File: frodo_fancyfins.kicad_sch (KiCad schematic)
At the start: 64 parts, among them J1 Molex MicroFit 2x3, J2 Molex MicroFit 2x3, J3 U.FL, J4 SWD Header, Q1 AO3400A, U15 AZ1117-5.0, U16 AZ1117-5.0, U17 W25Q128JVP, U18 AS321KTR-G1, U2 MCP2562-E-SN, U3 AZ1117-3.3, U4 STM32F103RCTx, Y1 8MHz 12pF

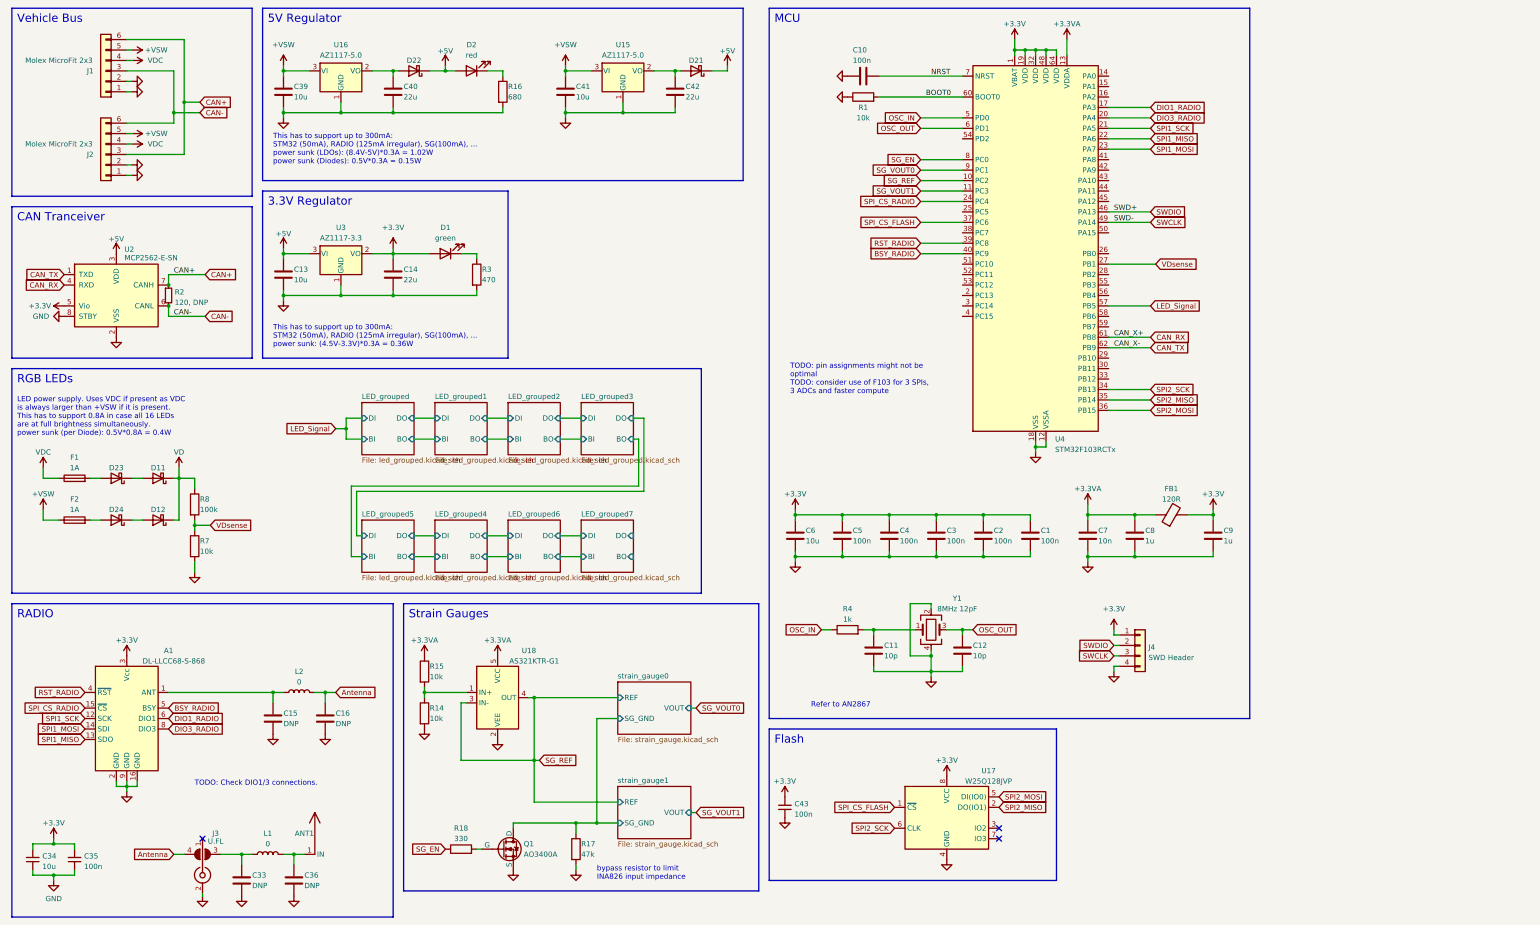
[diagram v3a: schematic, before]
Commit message: implement changes from rev 0 to rev 1
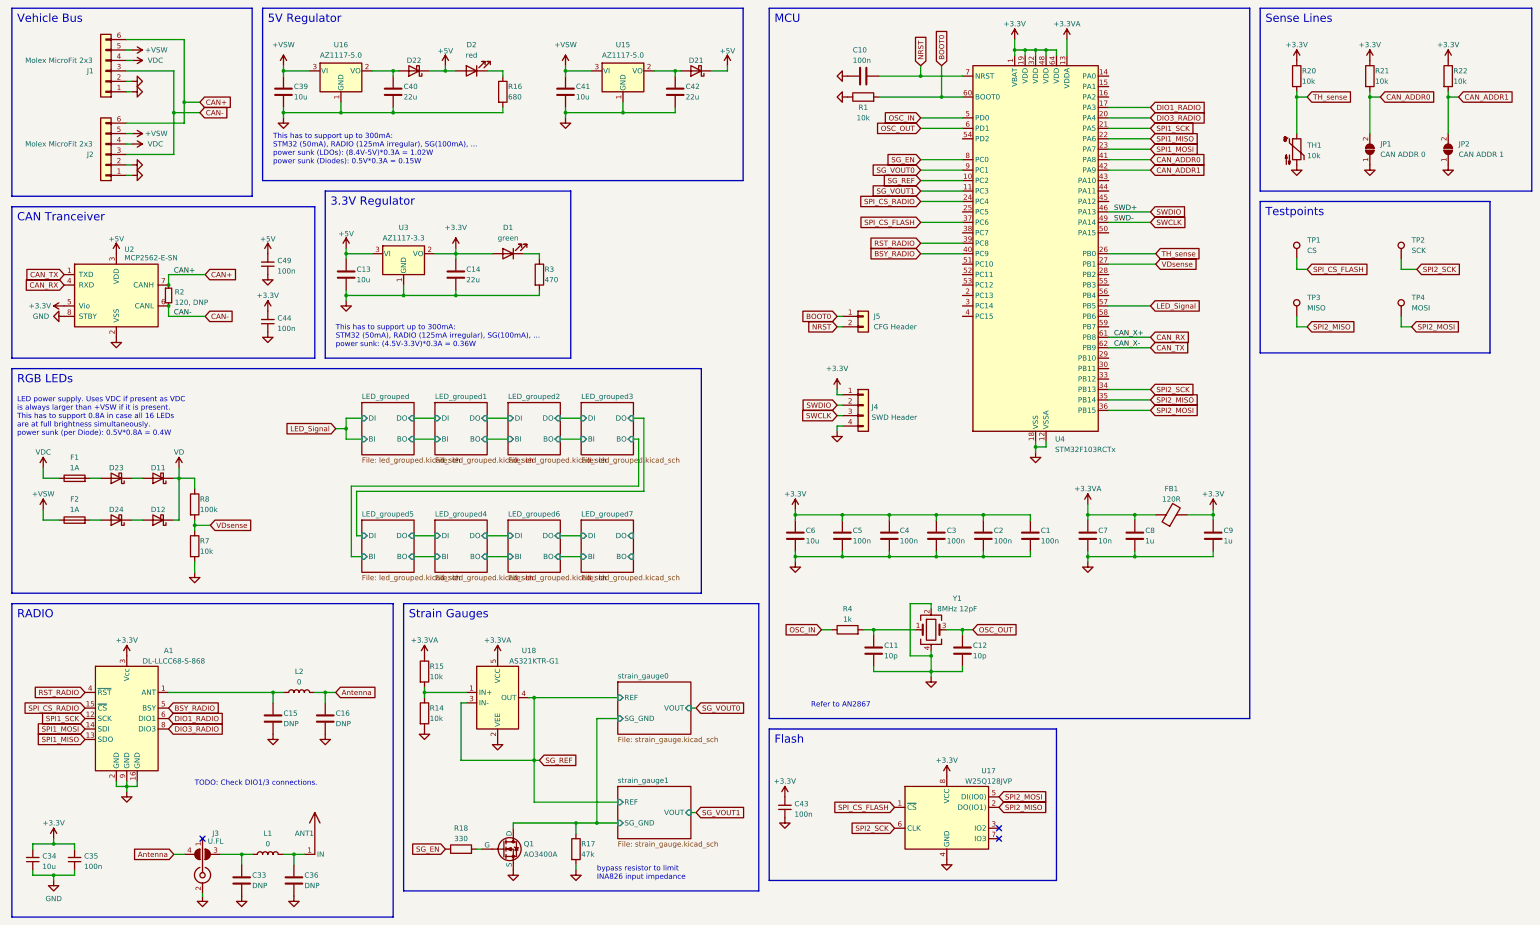
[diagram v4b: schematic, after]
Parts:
- added C44, C49: 100n, Capacitor_SMD:C_0402_1005Metric_Pad0.74x0.62mm_HandSolder, symbol Device:C_Small
- added J5: CFG Header, Connector_PinHeader_2.54mm:PinHeader_1x02_P2.54mm_Vertical, symbol Connector_Generic:Conn_01x02
- added JP1: CAN ADDR 0, Jumper:SolderJumper-2_P1.3mm_Open_RoundedPad1.0x1.5mm, symbol Jumper:SolderJumper_2_Open
- added JP2: CAN ADDR 1, Jumper:SolderJumper-2_P1.3mm_Open_RoundedPad1.0x1.5mm, symbol Jumper:SolderJumper_2_Open
- added R20, R21, R22: 10k, Resistor_SMD:R_0603_1608Metric_Pad0.98x0.95mm_HandSolder, symbol Device:R
- added TH1: 10k, Resistor_SMD:R_0603_1608Metric_Pad0.98x0.95mm_HandSolder, symbol Device:Thermistor_NTC
- added TP1: CS, TestPoint:TestPoint_Pad_D2.0mm, symbol Connector:TestPoint
- added TP2: SCK, TestPoint:TestPoint_Pad_D2.0mm, symbol Connector:TestPoint
- added TP3: MISO, TestPoint:TestPoint_Pad_D2.0mm, symbol Connector:TestPoint
- added TP4: MOSI, TestPoint:TestPoint_Pad_D2.0mm, symbol Connector:TestPoint
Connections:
- net +3.3V: now also C44.2, R20.1, R21.1, R22.1
- net +5V: now also C49.2
- net BOOT0: now also J5.1 (Pin_1)
- net CAN+: now also J2.6 (Pin_6); no longer J2.3 (Pin_3)
- net CAN-: now also J2.3 (Pin_3); no longer J2.6 (Pin_6)
- net GND: now also Q1.2 (S), C44.1, C49.1, JP1.1 (A), JP2.1 (A), TH1.2; no longer Q1.3 (S)
- net NRST: now also J5.2 (Pin_2)
- net SPI2_MISO: now also TP3.1
- net SPI2_MOSI: now also TP4.1
- net SPI2_SCK: now also TP2.1
- net SPI_CS_FLASH: now also TP1.1
- net strain_gauge0/SG_GND: now also Q1.3 (D); no longer Q1.1 (D)
- net TH_sense: now reaches U4.26 (PB0)
- net TH_sense: now also R20.2, TH1.1
- net CAN_ADDR0: now reaches U4.41 (PA8)
- net CAN_ADDR0: now also JP1.2 (B), R21.2
- net CAN_ADDR1: now reaches U4.42 (PA9)
- net CAN_ADDR1: now also JP2.2 (B), R22.2
- net at R18.2: now also Q1.1 (G); no longer Q1.2 (G)
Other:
- note added: "Sense Lines"
- note added: "Testpoints"
- note removed: "TODO: pin assignments might not be optimal TODO: consider use of F103 for 3 SPIs, 3 ADCs and faster compute"
- moved on the sheet: C13, C14, D1, J4, R3, U3

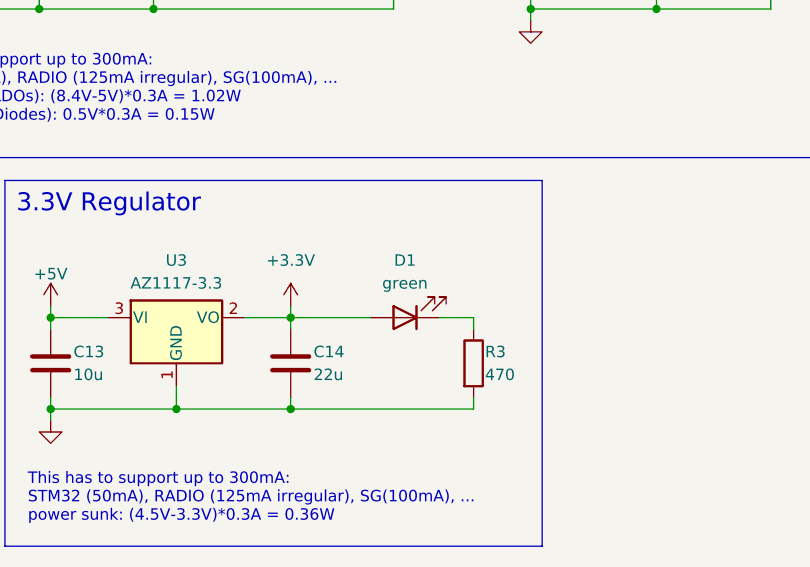
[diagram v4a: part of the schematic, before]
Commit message: add LCSC part numbers, tweak some footprints
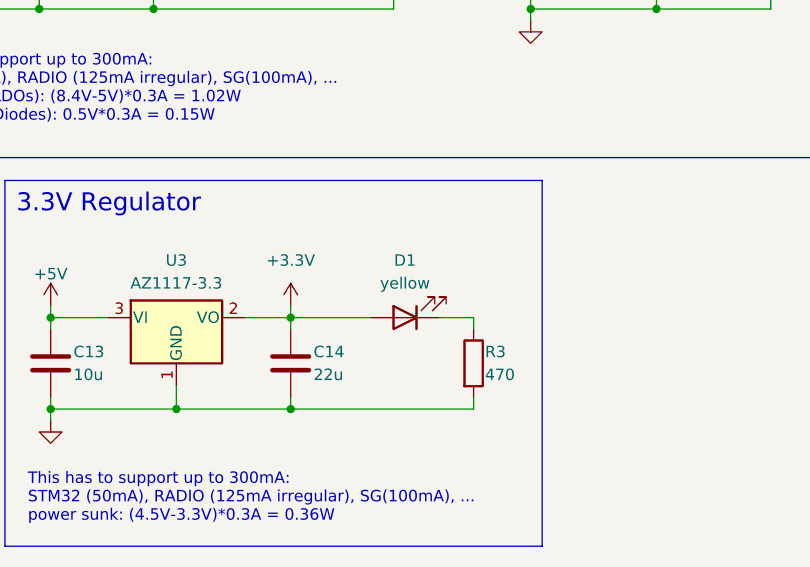
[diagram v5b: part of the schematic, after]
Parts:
- C1, C10, C2, C3, C35, C4, C43, C44, C49, C5: LCSC# (none) -> C307331
- C11, C12: LCSC# (none) -> C32949
- C13, C34, C39, C41, C6: LCSC# (none) -> C96446
- C14, C40, C42: LCSC# (none) -> C45783
- C7: LCSC# (none) -> C15195
- C8, C9: LCSC# (none) -> C15849
- D1: value green -> yellow; LCSC# (none) -> C72038; Manufacturer (none) -> Everlight Elec
- D11, D12, D21, D22, D23, D24: footprint Diode_SMD:D_SMA -> Diode_SMD:D_SOD-123F; LCSC# (none) -> C167645
- D2: LCSC# (none) -> C2286; Manufacturer (none) -> Hubei KENTO Elec
- F1, F2: footprint Fuse:Fuse_1812_4532Metric_Pad1.30x3.40mm_HandSolder -> Fuse:Fuse_1206_3216Metric_Pad1.42x1.75mm_HandSolder; Notes NOT FINAL FOOTPRINT! -> self-assembly PTC
- FB1: LCSC# (none) -> C1002; Manufacturer (none) -> Sunlord
- Q1: LCSC# (none) -> C20917; Manufacturer (none) -> Alpha & Omega Semicon
- R1, R14, R15, R7: LCSC# (none) -> C25744; Manufacturer (none) -> UNI-ROYAL(Uniroyal Elec)
- R16: LCSC# (none) -> C23228; Manufacturer (none) -> UNI-ROYAL(Uniroyal Elec)
- R17: LCSC# (none) -> C25792; Manufacturer (none) -> UNI-ROYAL(Uniroyal Elec)
- R18: LCSC# (none) -> C25104; Manufacturer (none) -> UNI-ROYAL(Uniroyal Elec)
- R3: LCSC# (none) -> C25117; Manufacturer (none) -> UNI-ROYAL(Uniroyal Elec)
- R4: LCSC# (none) -> C11702; Manufacturer (none) -> UNI-ROYAL(Uniroyal Elec)
- R8: LCSC# (none) -> C25741; Manufacturer (none) -> UNI-ROYAL(Uniroyal Elec)
- TH1: Notes (none) -> self-assemble?
- U15, U16: LCSC# (none) -> C526405; Manufacturer (none) -> Diodes Incorporated
- U17: LCSC# (none) -> C190862; Manufacturer (none) -> Winbond Elec
- U18: LCSC# (none) -> C144156; Manufacturer (none) -> Diodes Incorporated
- U2: LCSC# (none) -> C191417; Manufacturer (none) -> Microchip Tech
- U3: LCSC# (none) -> C110474; Manufacturer (none) -> Diodes Incorporated
- U4: LCSC# (none) -> C8323; Manufacturer (none) -> STMicroelectronics
- Y1: LCSC# (none) -> C2149245; Manufacturer (none) -> JYJE
